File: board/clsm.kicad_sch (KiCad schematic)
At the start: 2 parts, among them U1 STM32F103C8Tx, U2 MAX485E

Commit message: [01-4-2024] Adding Several Page Sheet
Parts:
- removed U2: MAX485E, symbol Interface_UART:MAX485E
- added C1: C, Capacitor_SMD:C_01005_0402Metric_Pad0.57x0.30mm_HandSolder, symbol Device:C
- added C2: C_Polarized_US, Capacitor_SMD:CP_Elec_5x3, symbol Device:C_Polarized_US
- added D1: IR26-21C_L110_TR8, LED_SMD:LED_1206_3216Metric, symbol LED:IR26-21C_L110_TR8
- added J1: Conn_ARM_SWD_TagConnect_TC2030-NL, Connector:Tag-Connect_TC2030-IDC-NL_2x03_P1.27mm_Vertical, symbol Connector:Conn_ARM_SWD_TagConnect_TC2030-NL
- added J2: Micro_SD_Card, Connector_Card:microSD_HC_Wuerth_693072010801, symbol Connector:Micro_SD_Card
- added J3: USB_B, Connector_USB:USB_B_OST_USB-B1HSxx_Horizontal, symbol Connector:USB_B
- added R1: R_US, Resistor_SMD:R_0805_2012Metric_Pad1.20x1.40mm_HandSolder, symbol Device:R_US
- added SW1: SW_Omron_B3FS, Button_Switch_SMD:SW_SPST_Omron_B3FS-100xP, symbol Switch:SW_Omron_B3FS
- added U6: DRV8844PWPR, PWP28_5P18X3P1, symbol 2024-04-30_14-35-36:DRV8844PWPR
- added U7: TMC2208-LA, Package_DFN_QFN:TQFN-32-1EP_5x5mm_P0.5mm_EP3.4x3.4mm_ThermalVias, symbol Driver_Motor:TMC2208-LA
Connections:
- new net: U7.18 (GND), U7.3 (GND)
- new net: U7.22 (VS), U7.28 (VS)
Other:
- added sheet Comunication_Unit (Comunication_Unit.kicad_sch)
- added sheet IO_Unit (IO_Unit.kicad_sch)
- added sheet Temp_Input_Unit (TemperatureInput.kicad_sch)
- company: (none) -> AHAH_TERROR
- title: (none) -> Main Schematic

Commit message: [6-5-2024] Create I/O
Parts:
- added C10, C11, C12, C13, C14: 100n, Capacitor_SMD:C_01005_0402Metric_Pad0.57x0.30mm_HandSolder, symbol Device:C
- added C7: 22u, Capacitor_SMD:CP_Elec_5x3, symbol Device:C_Polarized_US
- added C8: 100u/10v, Capacitor_SMD:CP_Elec_5x3, symbol Device:C_Polarized_US
- added C9: 270u/10v, Capacitor_SMD:CP_Elec_5x3, symbol Device:C_Polarized_US
- added D3: SS34, Diode_SMD:D_SMA, symbol Diode:SS34
- added J4: VBUS, TerminalBlock_TE-Connectivity:TerminalBlock_TE_282834-2_1x02_P2.54mm_Horizontal, symbol Connector:Screw_Terminal_01x02
- added J5: VBat, Connector_PinHeader_2.54mm:PinHeader_1x02_P2.54mm_Vertical, symbol Connector_Generic:Conn_01x02
- added J6: Conn_ARM_JTAG_SWD_10, Connector_PinHeader_1.27mm:PinHeader_2x05_P1.27mm_Horizontal, symbol Connector:Conn_ARM_JTAG_SWD_10
- added J7: BOOT0, Connector_PinSocket_2.54mm:PinSocket_1x03_P2.54mm_Vertical, symbol Connector_Generic:Conn_01x03
- added J8: BOOT1, Connector_PinSocket_2.54mm:PinSocket_1x03_P2.54mm_Vertical, symbol Connector_Generic:Conn_01x03
- added L1: 68u, Inductor_SMD:L_7.3x7.3_H3.5, symbol Device:L
- added U11: LM2596S-5, Package_TO_SOT_SMD:TO-263-5_TabPin3, symbol Regulator_Switching:LM2596S-5
- added U5: AMS1117-3.3, Package_TO_SOT_SMD:SOT-223-3_TabPin2, symbol Regulator_Linear:AMS1117-3.3
- C1: value C -> 100n
- C2: value C_Polarized_US -> 10u
- SW1: value SW_Omron_B3FS -> Reset
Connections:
- net +3V3: now also C1.1, U1.24 (VDD), U1.36 (VDD), U1.48 (VDD), U1.9 (VDDA), C10.1, C11.1, C13.1, C7.1, J7.3 (Pin_3), J8.3 (Pin_3), U5.2 (VO)
- net +BATT: now also U1.1 (VBAT), C12.1, J5.2 (Pin_2)
- net +5V: now reaches C2.1
- net +5V: now also C9.1, J6.1 (VTref), L1.2, U11.4 (FB), U5.3 (VI)
- net GND: now reaches C2.2
- net GND: now also C1.2, SW1.2, U1.23 (VSS), U1.35 (VSS), U1.47 (VSS), U1.8 (VSSA), C10.2, C11.2, C12.2, C13.2, C14.2, C7.2, C8.2, C9.2, D3.2 (A), J4.1 (Pin_1), J5.1 (Pin_1), J6.3 (GND), J6.5 (GND), J6.9 (GNDDetect), J7.1 (Pin_1), J8.1 (Pin_1), U11.3 (GND), U11.5 (~{ON}/OFF), U5.1 (GND)
- net nrst: now reaches SW1.1
- net nrst: now also U1.7 (NRST), C14.1, J6.10 (~{RESET})
- net ADC12_IN1: now reaches U1.11 (PA1)
- net ADC12_IN2: now reaches U1.12 (PA2)
- net ADC12_IN3: now reaches U1.13 (PA3)
- net SPI1_NSS: now reaches U1.14 (PA4)
- net SPI1_SCK: now reaches U1.15 (PA5)
- net SPI1_MISO: now reaches U1.16 (PA6)
- net SPI1_MOSI: now reaches U1.17 (PA7)
- net ADC12_IN8: now reaches U1.18 (PB0)
- net ADC12_IN9: now reaches U1.19 (PB1)
- net boot1: now reaches U1.20 (PB2)
- net boot1: now also J8.2 (Pin_2)
- net USB_DM: now reaches U1.32 (PA11)
- net USB_DP: now reaches U1.33 (PA12)
- net I2C1_SCL: now reaches U1.42 (PB6)
- net I2C1_SDA: now reaches U1.43 (PB7)
- net boot0: now reaches U1.44 (BOOT0)
- net boot0: now also J7.2 (Pin_2)
- net CAN_RX: now reaches U1.45 (PB8)
- net CAN_TX: now reaches U1.46 (PB9)
- new net: D3.1 (K), L1.1, U11.2 (OUT)
- new net SWCLK: J6.4 (SWCLK/TCK)
- new net SWDIO: J6.2 (SWDIO/TMS)
- new net SWO: J6.6 (SWO/TDO)
- new net TDI: J6.8 (NC/TDI)
- new net VBUS: C8.1, J4.2 (Pin_2), U11.1 (VIN)
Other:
- added sheet Simulation (Simulation.kicad_sch)
- sheet IO_Unit ports: added INTA_MCP23017, INTB_MCP23017, SCK_MCP23017, SDA_MCP23017; removed none
- moved on the sheet: C2, D1, J1, J2, J3, R1, SW1, U1, U6A, U6B, U7

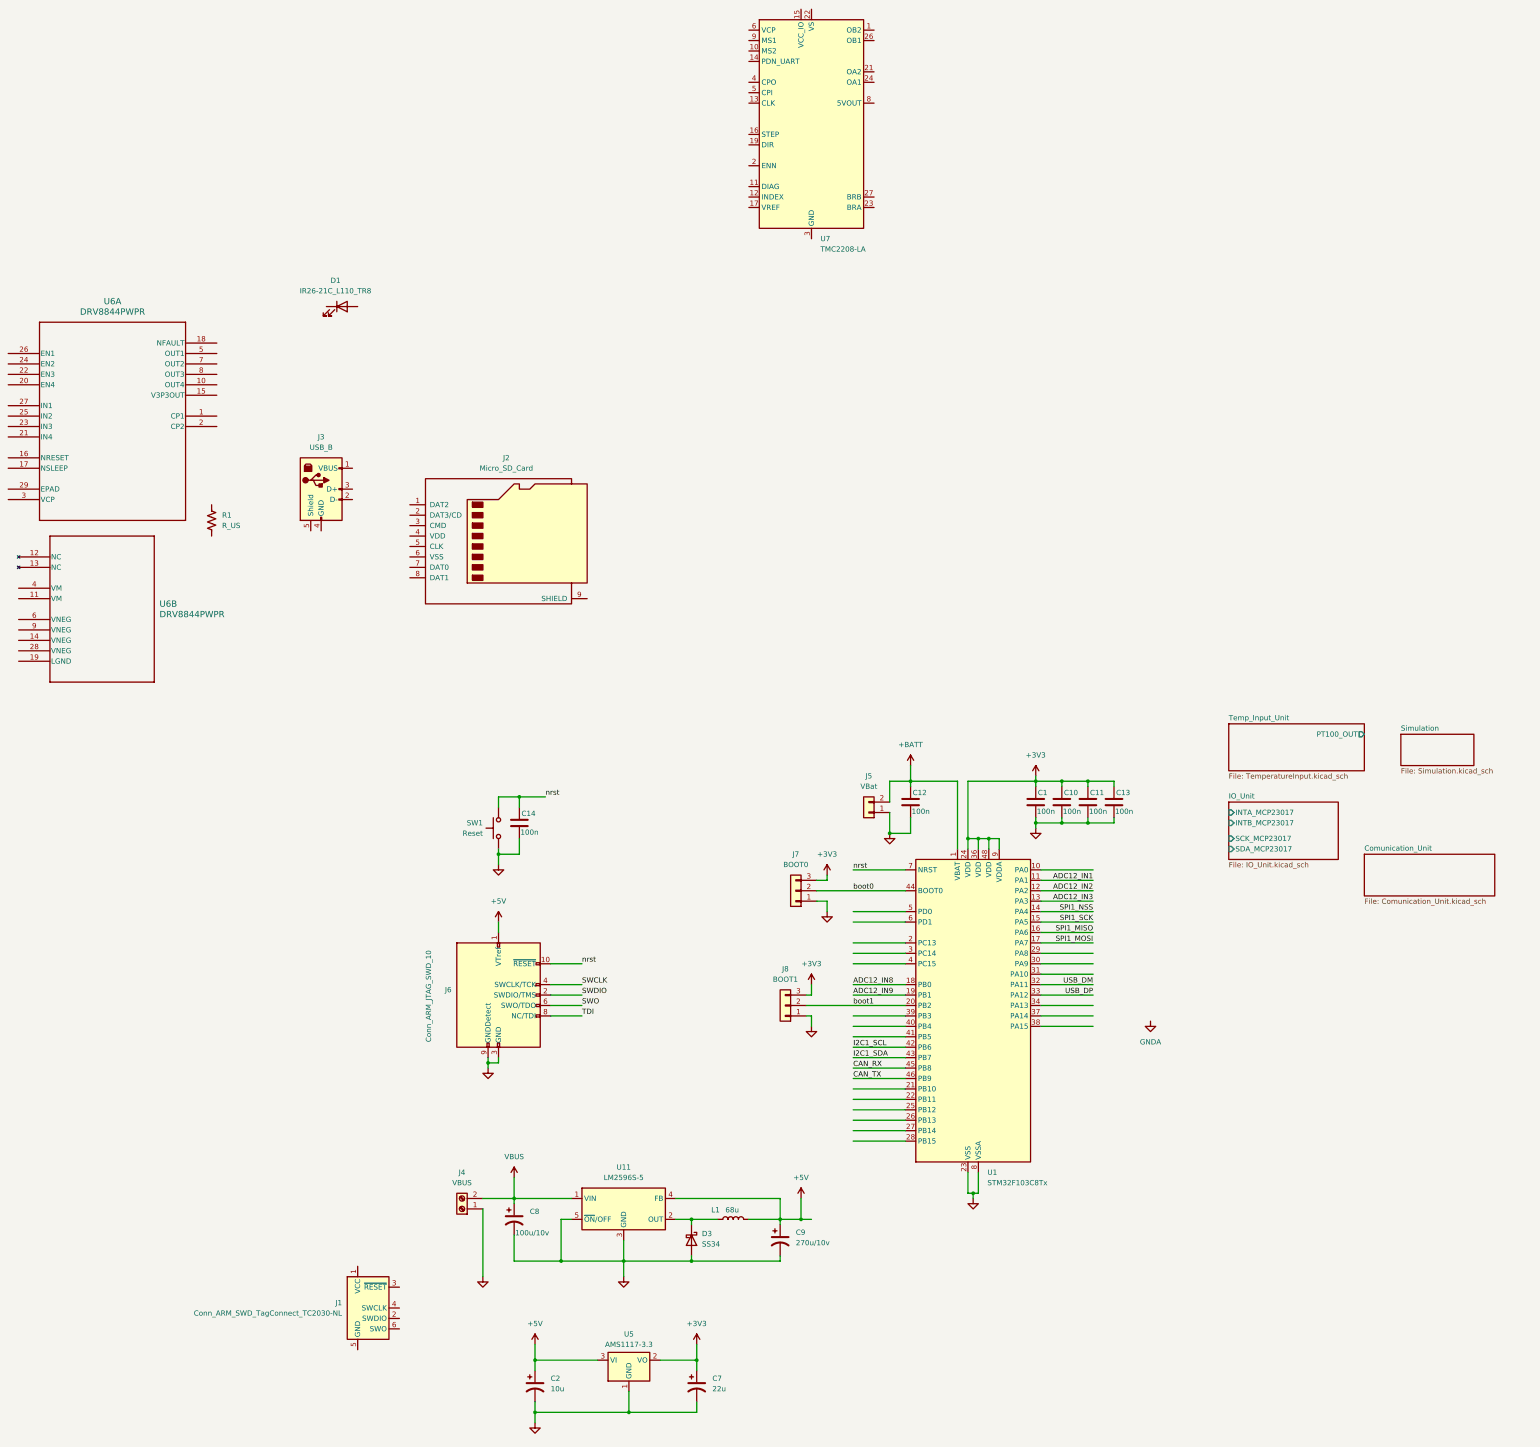
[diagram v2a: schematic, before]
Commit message: [23-5-2024] adding TMC2208 Motor Driver Schematic
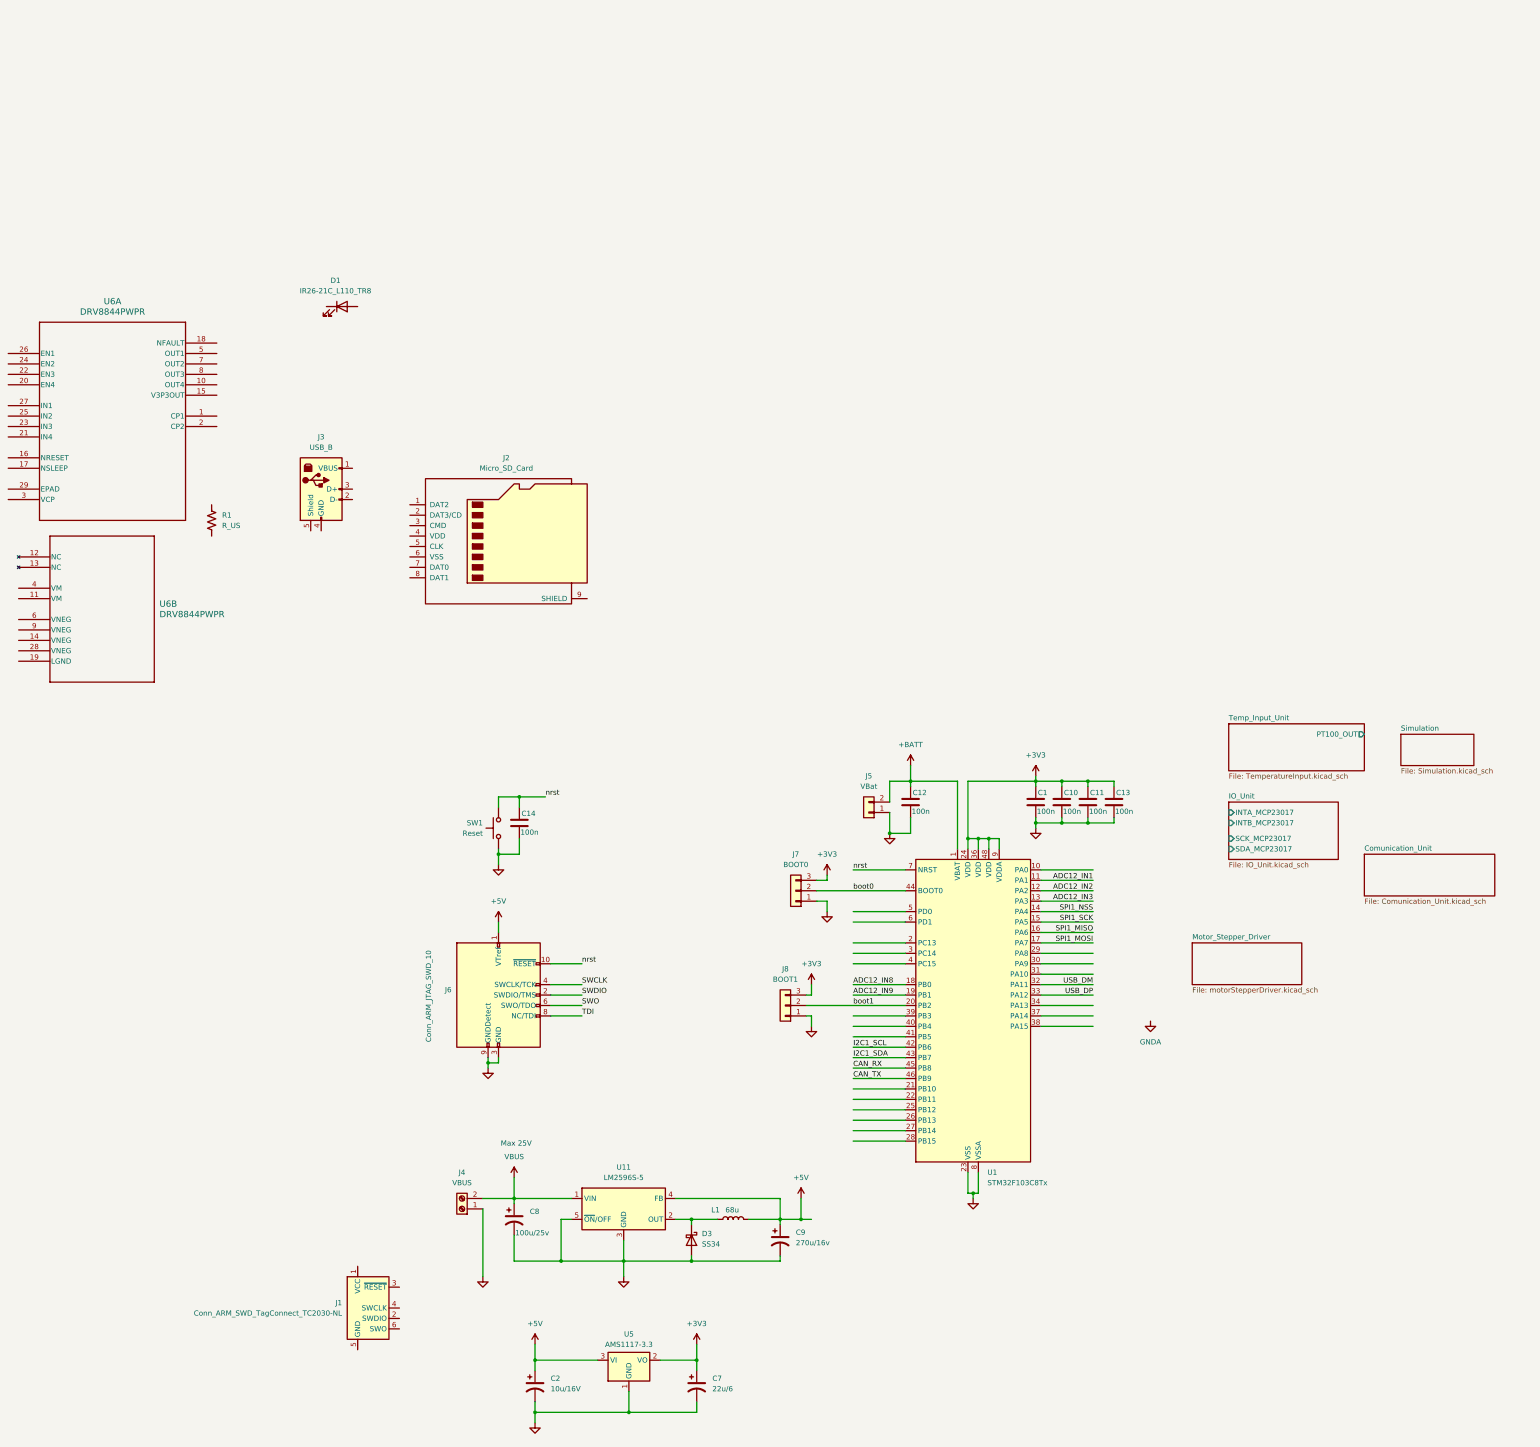
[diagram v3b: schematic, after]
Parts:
- removed U7: TMC2208-LA, Package_DFN_QFN:TQFN-32-1EP_5x5mm_P0.5mm_EP3.4x3.4mm_ThermalVias, symbol Driver_Motor:TMC2208-LA
- C2: value 10u -> 10u/16V
- C7: value 22u -> 22u/6
- C8: value 100u/10v -> 100u/25v
- C9: value 270u/10v -> 270u/16v
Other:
- added sheet Motor_Stepper_Driver (motorStepperDriver.kicad_sch)
- note added: "Max 25V"
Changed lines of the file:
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@@
 		)
 	)
+	(text "Max 25V\n"
+		(exclude_from_sim no)
+		(at 37.338 126.492 0)
+		(effects
+			(font
+				(size 1.27 1.27)
+			)
+		)
+	)
 	(label "ADC12_IN1"
 		(at 177.8 62.23 180)
@@
 			)
 		)
-		(property "Value" "10u"
+		(property "Value" "10u/16V"
 			(at 45.72 186.0549 0)
 			(effects
@@
 	)
 	(symbol
-		(lib_id "Driver_Motor:TMC2208-LA")
-		(at 109.22 -121.92 0)
-		(unit 1)
-		(exclude_from_sim yes)
-		(in_bom yes)
-		(on_board yes)
-		(dnp no)
-		(fields_autoplaced yes)
-		(property "Reference" "U7"
-			(at 111.4141 -93.98 0)
-			(effects
-				(font
-					(size 1.27 1.27)
-				)
-				(justify left)
-			)
-		)
-		(property "Value" "TMC2208-LA"
-			(at 111.4141 -91.44 0)
-			(effects
-				(font
-					(size 1.27 1.27)
-				)
-				(justify left)
-			)
-		)
-		(property "Footprint" "Package_DFN_QFN:TQFN-32-1EP_5x5mm_P0.5mm_EP3.4x3.4mm_ThermalVias"
-			(at 109.22 -81.28 0)
-			(effects
-				(font
-					(size 1.27 1.27)
-				)
-				(hide yes)
-			)
-		)
-		(property "Datasheet" "https://www.analog.com/media/en/technical-documentation/data-sheets/TMC2202_TMC2208_TMC2224_datasheet_rev1.13.pdf"
-			(at 109.22 -76.2 0)
-			(effects
-				(font
-					(size 1.27 1.27)
-				)
-				(hide yes)
-			)
-		)
-		(property "Description" "Standalone driver for two-phase bipolar stepper motor, 2A, 4.75… 36V, UART, internal FETs, QFN28"
-			(at 109.22 -121.92 0)
-			(effects
-				(font
-					(size 1.27 1.27)
-				)
-				(hide yes)
-			)
-		)
-		(pin "28"
-		)
-		(pin "25"
-		)
-		(pin "4"
-		)
-		(pin "13"
-		)
-		(pin "14"
-		)
-		(pin "23"
-		)
-		(pin "19"
-		)
-		(pin "18"
-		)
-		(pin "16"
-		)
-		(pin "17"
-		)
-		(pin "5"
-		)
-		(pin "20"
-		)
-		(pin "6"
-		)
-		(pin "2"
-		)
-		(pin "8"
-		)
-		(pin "27"
-		)
-		(pin "1"
-		)
-		(pin "12"
-		)
-		(pin "26"
-		)
-		(pin "11"
-		)
-		(pin "10"
-		)
-		(pin "3"
-		)
-		(pin "24"
-		)
-		(pin "7"
-		)
-		(pin "9"
-		)
-		(pin "21"
-		)
-		(pin "15"
-		)
-		(pin "22"
-		)
-		(instances
-			(project "clsm"
-				(path "/508e0e3b-a744-4e88-93ea-e872e80e580c"
-					(reference "U7")
-					(unit 1)
-				)
-			)
-		)
-	)
-	(symbol
 		(lib_id "Connector_Generic:Conn_01x03")
 		(at 102.87 92.71 180)
@@
 			)
 		)
-		(property "Value" "270u/10v"
+		(property "Value" "270u/16v"
 			(at 105.41 150.4949 0)
 			(effects
@@
 			)
 		)
-		(property "Value" "22u"
+		(property "Value" "22u/6"
 			(at 85.09 186.0549 0)
 			(effects
@@
 			)
 		)
-		(property "Value" "100u/10v"
+		(property "Value" "100u/25v"
 			(at 37.084 148.082 0)
 			(effects
@@
 				)
 			)
+		)
+	)
+	(sheet
+		(at 201.93 77.47)
+		(size 26.67 10.16)
+		(fields_autoplaced yes)
+		(stroke
+			(width 0.1524)
+			(type solid)
+		)
+		(fill
+			(color 0 0 0 0.0000)
+		)
+		(property "Sheetname" "Motor_Stepper_Driver"
+			(at 201.93 76.7584 0)
+			(effects
+				(font
+					(size 1.27 1.27)
+				)
+				(justify left bottom)
+			)
+		)
+		(property "Sheetfile" "motorStepperDriver.kicad_sch"
+			(at 201.93 88.2146 0)
+			(effects
+				(font
+					(size 1.27 1.27)
+				)
+				(justify left top)
+			)
+		)
+		(instances
+			(project "clsm"
+				(path "/508e0e3b-a744-4e88-93ea-e872e80e580c"
+					(page "6")
+				)
+			)

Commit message: [23-5-2024] add micro sd card connector and MAX31856 Thermocouple driver
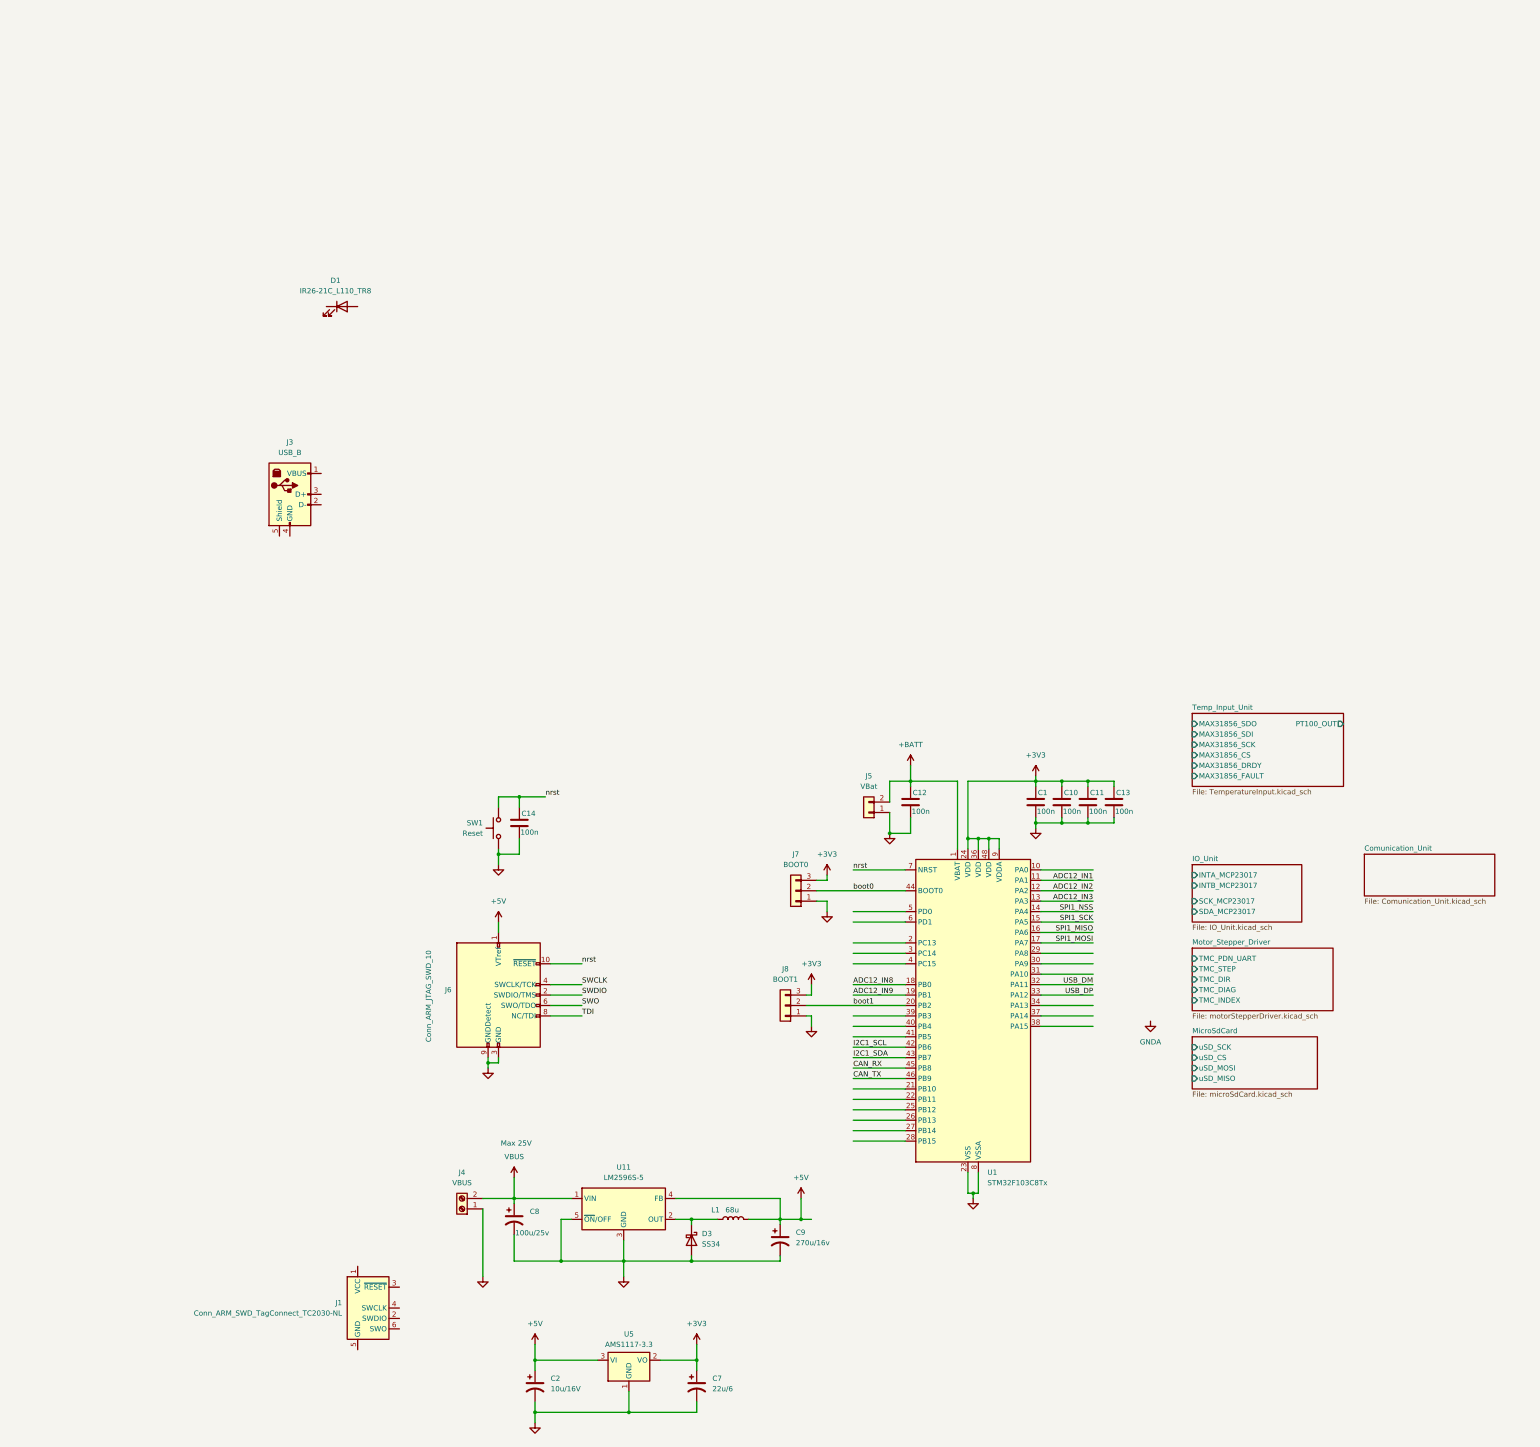
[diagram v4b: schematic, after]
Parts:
- removed J2: Micro_SD_Card, Connector_Card:microSD_HC_Wuerth_693072010801, symbol Connector:Micro_SD_Card
- removed R1: R_US, Resistor_SMD:R_0805_2012Metric_Pad1.20x1.40mm_HandSolder, symbol Device:R_US
- removed U6: DRV8844PWPR, PWP28_5P18X3P1, symbol 2024-04-30_14-35-36:DRV8844PWPR
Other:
- removed sheet Simulation
- added sheet MicroSdCard (microSdCard.kicad_sch)
- sheet Motor_Stepper_Driver ports: added TMC_DIAG, TMC_DIR, TMC_INDEX, TMC_PDN_UART, TMC_STEP; removed none
- sheet Temp_Input_Unit ports: added MAX31856_CS, MAX31856_DRDY, MAX31856_FAULT, MAX31856_SCK, MAX31856_SDI, MAX31856_SDO; removed none
- moved on the sheet: J3
